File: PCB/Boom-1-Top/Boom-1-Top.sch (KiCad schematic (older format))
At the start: 983 parts, among them J1 DEBUG, J10 PIC_DEBUG, J11 PIC_DEBUG, J12 PIC_DEBUG, J13 PIC_DEBUG, J14 PIC_DEBUG, J15 USB_B_Micro, J16 SD_Card, J17 BT_DEBUG, J18 12V Supply, J19 3V3 Bypass, J2 MIDI IN, J20 5V Bypass, J21 Env +12V Supply, J22 Env -12V Supply, J23 OLEDConn, J3 MIDI OUT, J37 Osc1Conn, J38 Osc2Conn, J39 SubNoiseConn, J4 PIC_DEBUG, J40 FiltConn2, J41 EnvGenConn2, J42 EnvGenConn1, J43 FXConn1, J44 FiltConn1, J45 FXConn2, J46 EnvGenConn3, J5 PIC_DEBUG, J6 PIC_DEBUG, J7 PIC_DEBUG, J8 PIC_DEBUG, J9 PIC_DEBUG, Q1 AO3401A, Q2 AO3401A, SW1 Osc1SawEncoder, SW10 SubToOsc2FiltEncoder, SW11 Osc1ToOsc2FiltEncoder, SW12 Osc1FiltFreqEncoder, SW13 Osc2FiltFreqEncoder, SW14 SubFiltFreqEncoder, SW15 OscFiltEnvAttackEncoder, SW16 SubFiltEnvAttackEncoder, SW17 Osc1FiltResEncoder, SW18 Osc2FiltResEncoder, SW19 SubFiltResEncoder, SW2 Osc1SqrEncoder, SW20 OscFiltEnvDecayEncoder, SW21 SubFiltEnvDecayEncoder, SW22 OscFiltEnvSustainEncoder, SW23 SubFiltEnvSustainEncoder, SW24 Osc1DriveEncoder, SW25 Osc2DistortionEncoder, SW26 OscFiltEnvReleaseEncoder, SW27 SubFiltEnvReleaseEncoder, SW28 FXWetDryEncoder, SW29 SubAmpEnvAttackEncoder, SW3 Rotary_Encoder, SW30 OscAmpEnvAttackEncoder, SW31 FXControl1Encoder, SW32 SubAmpEnvDecayEncoder, SW33 OscAmpEnvDecayEncoder, SW34 FXControl2Encoder, SW35 SubAmpEnvSustainEncoder, SW36 OscAmpEnvSustainEncoder, SW37 FXControl3Encoder, SW38 FXFeedbackEncoder, SW39 SubAmpEnvReleaseEncoder, SW4 Rotary_Encoder_Switch, SW40 OscAmpEnvReleaseEncoder, SW41 Reset, SW42 SW_Push, SW43 Reset, SW44 SW_Push, SW45 SW_Push, SW46 SW_Push, SW47 SW_Push, SW48 SW_Push, SW49 SW_Push, SW5 Rotary_Encoder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

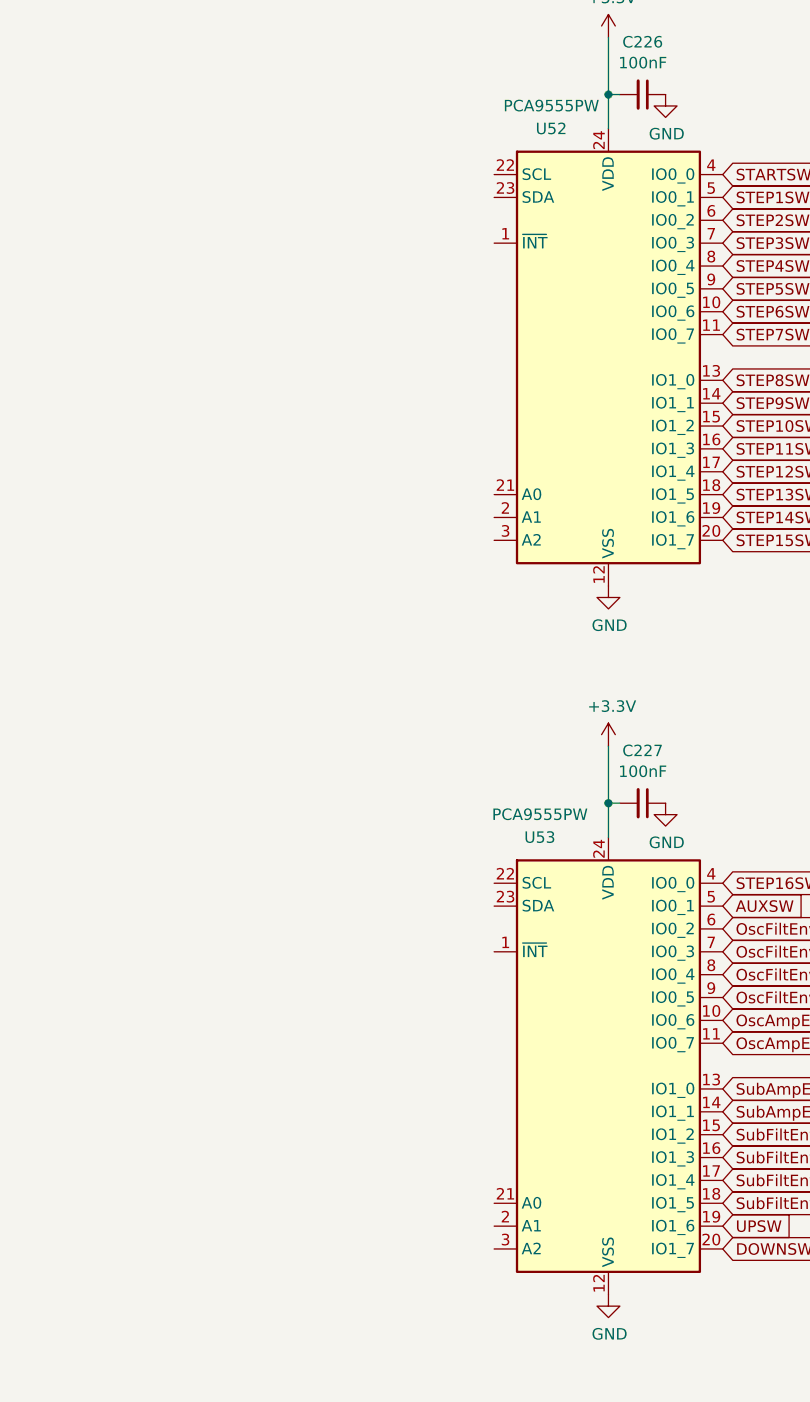
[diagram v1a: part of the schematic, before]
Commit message: - i2c lines for GPIO expanders - Tidied up 5v supply copper connection
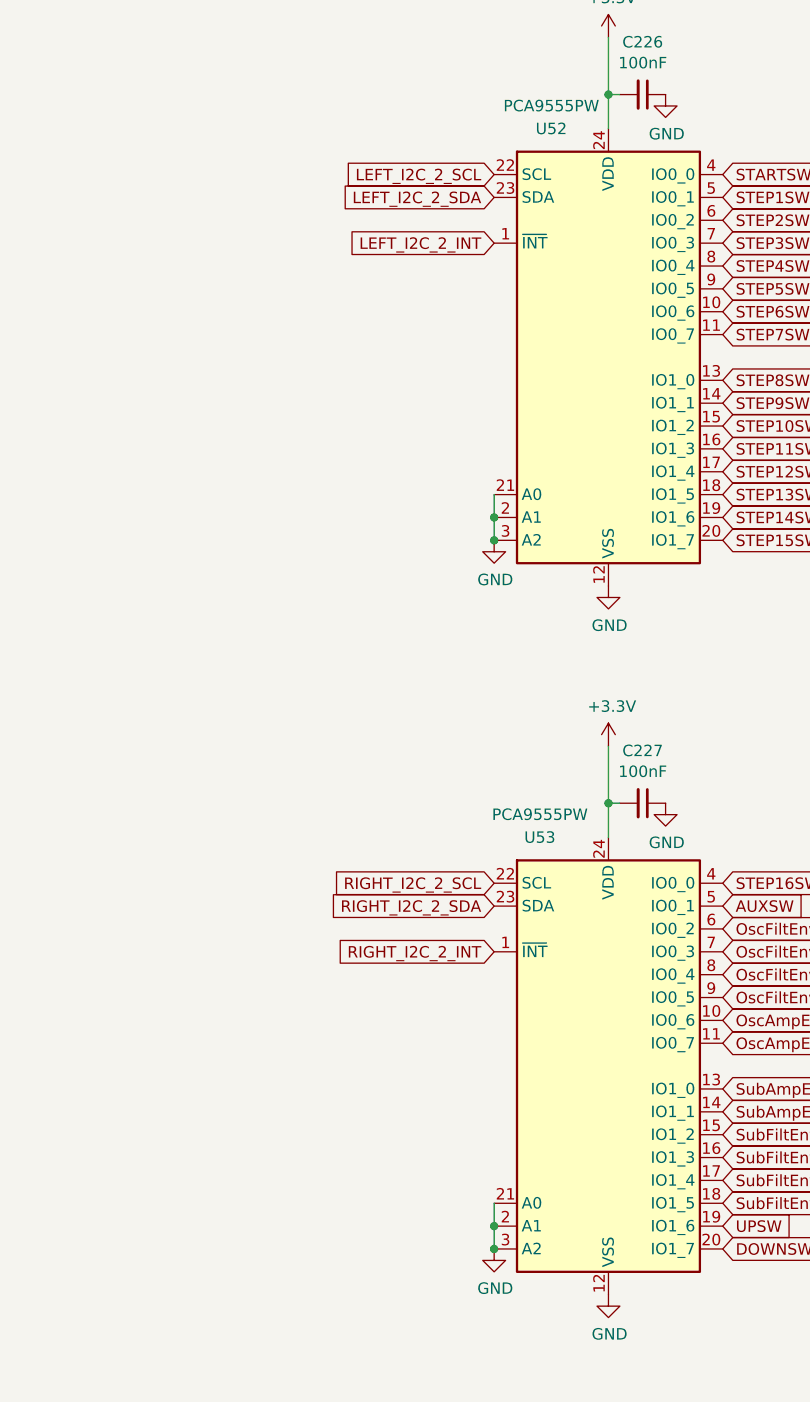
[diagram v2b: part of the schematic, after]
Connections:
- net GND: now also U52.2 (A1), U52.21 (A0), U52.3 (A2), U53.2 (A1), U53.21 (A0), U53.3 (A2)
- net LEFT_I2C_2_INT: now also U52.1 (~INT)
- net LEFT_I2C_2_SCL: now also U52.22 (SCL)
- net LEFT_I2C_2_SDA: now also U52.23 (SDA)
- net RIGHT_I2C_2_INT: now also U53.1 (~INT)
- net RIGHT_I2C_2_SCL: now also U53.22 (SCL)
- net RIGHT_I2C_2_SDA: now also U53.23 (SDA)
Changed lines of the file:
@@
 Wire Wire Line
 	5300 8800 5500 8800
+Text GLabel 21700 40750 0    50   Input ~ 0
+LEFT_I2C_2_SCL
+Text GLabel 21700 40850 0    50   Input ~ 0
+LEFT_I2C_2_SDA
+Text GLabel 21700 41050 0    50   Input ~ 0
+LEFT_I2C_2_INT
+Text GLabel 21700 43850 0    50   Input ~ 0
+RIGHT_I2C_2_SCL
+Text GLabel 21700 43950 0    50   Input ~ 0
+RIGHT_I2C_2_SDA
+Text GLabel 21700 44150 0    50   Input ~ 0
+RIGHT_I2C_2_INT
+$Comp
+L power:GND #PWR?
+U 1 1 6122B540
+P 21700 45450
+F 0 "#PWR?" H 21700 45200 50  0001 C CNN
+F 1 "GND" H 21705 45277 50  0000 C CNN
+F 2 "" H 21700 45450 50  0001 C CNN
+F 3 "" H 21700 45450 50  0001 C CNN
+	1    21700 45450
+	1    0    0    -1
+$EndComp
+Wire Wire Line
+	21700 45250 21700 45350
+Connection ~ 21700 45450
+Connection ~ 21700 45350
+Wire Wire Line
+	21700 45350 21700 45450
+$Comp
+L power:GND #PWR?
+U 1 1 617418BC
+P 21700 42350
+F 0 "#PWR?" H 21700 42100 50  0001 C CNN
+F 1 "GND" H 21705 42177 50  0000 C CNN
+F 2 "" H 21700 42350 50  0001 C CNN
+F 3 "" H 21700 42350 50  0001 C CNN
+	1    21700 42350
+	1    0    0    -1
+$EndComp
+Wire Wire Line
+	21700 42150 21700 42250
+Connection ~ 21700 42350
+Connection ~ 21700 42250
+Wire Wire Line
+	21700 42250 21700 42350
 $EndSCHEMATC

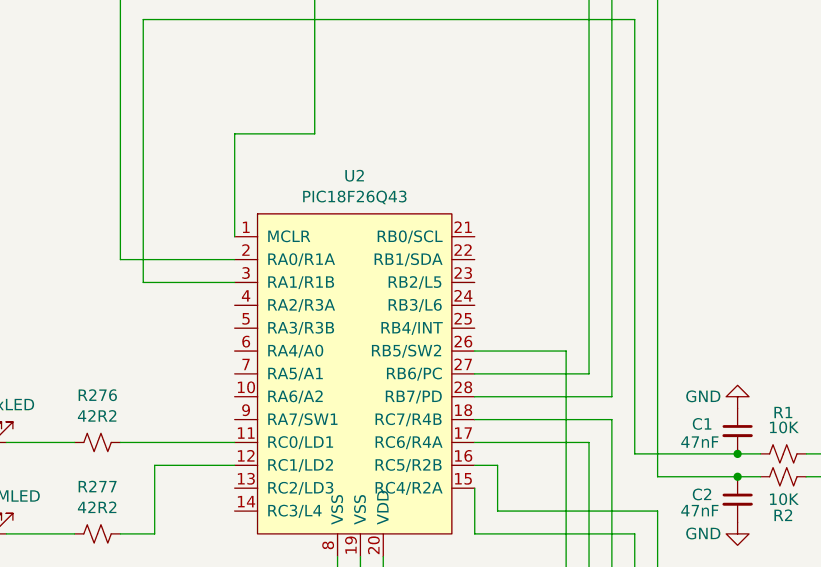
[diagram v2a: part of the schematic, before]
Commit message: First i2c line for PIC
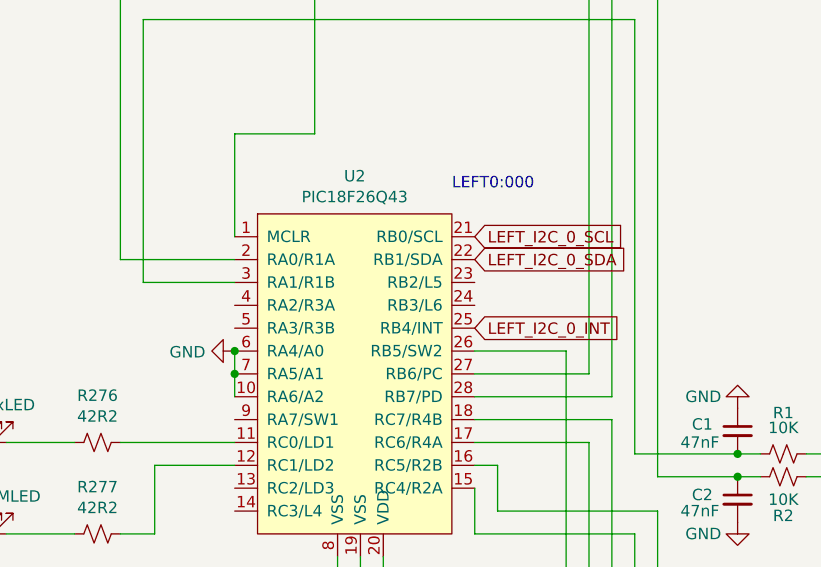
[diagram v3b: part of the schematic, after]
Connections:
- net GND: now also U2.10 (RA6/A2), U2.6 (RA4/A0), U2.7 (RA5/A1)
- net LEFT_I2C_0_INT: now also U2.25 (RB4/INT)
- net LEFT_I2C_0_SCL: now also U2.21 (RB0/SCL)
- net LEFT_I2C_0_SDA: now also U2.22 (RB1/SDA)
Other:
- note added: "LEFT0:000"
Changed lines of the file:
@@
 RIGHT_I2C_2_INT
 $Comp
-L power:GND #PWR?
+L power:GND #PWR0901
 U 1 1 6122B540
 P 21700 45450
-F 0 "#PWR?" H 21700 45200 50  0001 C CNN
+F 0 "#PWR0901" H 21700 45200 50  0001 C CNN
 F 1 "GND" H 21705 45277 50  0000 C CNN
 F 2 "" H 21700 45450 50  0001 C CNN
@@
 	21700 45350 21700 45450
 $Comp
-L power:GND #PWR?
+L power:GND #PWR0902
 U 1 1 617418BC
 P 21700 42350
-F 0 "#PWR?" H 21700 42100 50  0001 C CNN
+F 0 "#PWR0902" H 21700 42100 50  0001 C CNN
 F 1 "GND" H 21705 42177 50  0000 C CNN
 F 2 "" H 21700 42350 50  0001 C CNN
@@
 Wire Wire Line
 	21700 42250 21700 42350
+Text GLabel 27300 4400 2    50   Input ~ 0
+LEFT_I2C_0_SCL
+Text GLabel 27300 4500 2    50   Input ~ 0
+LEFT_I2C_0_SDA
+Text GLabel 27300 4800 2    50   Input ~ 0
+LEFT_I2C_0_INT
+Text Notes 27200 4200 0    50   ~ 0
+LEFT0:000
+$Comp
+L power:GND #PWR?
+U 1 1 637C74D9
+P 26250 4900
+F 0 "#PWR?" H 26250 4650 50  0001 C CNN
+F 1 "GND" V 26255 4772 50  0000 R CNN
+F 2 "" H 26250 4900 50  0001 C CNN
+F 3 "" H 26250 4900 50  0001 C CNN
+	1    26250 4900
+	0    1    1    0
+$EndComp
+Wire Wire Line
+	26250 4900 26250 5000
+Connection ~ 26250 4900
+Connection ~ 26250 5000
+Wire Wire Line
+	26250 5000 26250 5100
 $EndSCHEMATC

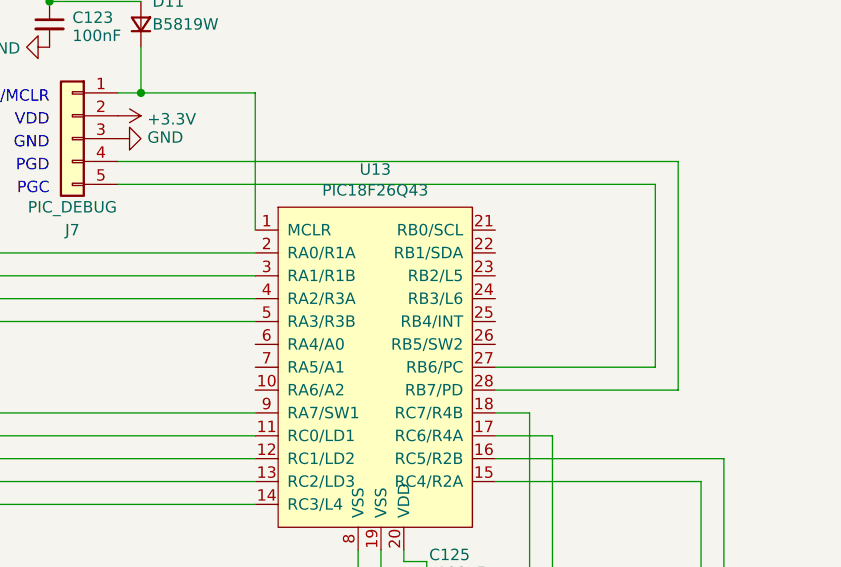
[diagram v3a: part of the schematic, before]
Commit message: i2c for PIC U13
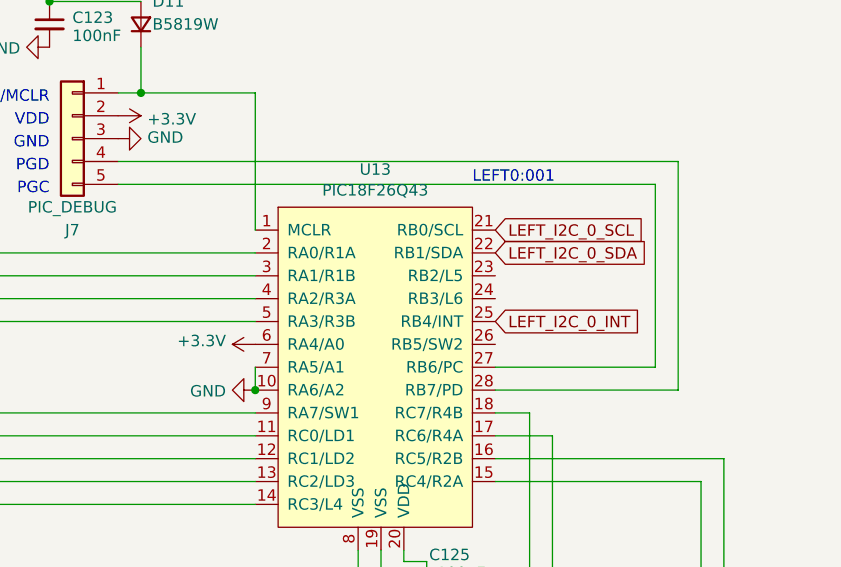
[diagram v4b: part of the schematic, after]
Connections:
- net +3V3: now also U13.6 (RA4/A0)
- net GND: now also U13.10 (RA6/A2), U13.7 (RA5/A1)
- net LEFT_I2C_0_INT: now also U13.25 (RB4/INT)
- net LEFT_I2C_0_SCL: now also U13.21 (RB0/SCL)
- net LEFT_I2C_0_SDA: now also U13.22 (RB1/SDA)
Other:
- note added: "LEFT0:001"
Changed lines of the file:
@@
 Wire Wire Line
 	21700 42250 21700 42350
-Text GLabel 27300 4400 2    50   Input ~ 0
-LEFT_I2C_0_SCL
-Text GLabel 27300 4500 2    50   Input ~ 0
-LEFT_I2C_0_SDA
-Text GLabel 27300 4800 2    50   Input ~ 0
-LEFT_I2C_0_INT
 Text Notes 27200 4200 0    50   ~ 0
 LEFT0:000
 $Comp
-L power:GND #PWR?
+L power:GND #PWR0903
 U 1 1 637C74D9
 P 26250 4900
-F 0 "#PWR?" H 26250 4650 50  0001 C CNN
+F 0 "#PWR0903" H 26250 4650 50  0001 C CNN
 F 1 "GND" V 26255 4772 50  0000 R CNN
 F 2 "" H 26250 4900 50  0001 C CNN
@@
 Wire Wire Line
 	26250 5000 26250 5100
+Text GLabel 27300 4800 2    50   Input ~ 0
+LEFT_I2C_0_INT
+Text GLabel 27300 4500 2    50   Input ~ 0
+LEFT_I2C_0_SDA
+Text GLabel 27300 4400 2    50   Input ~ 0
+LEFT_I2C_0_SCL
+Text Notes 35800 2200 0    50   ~ 0
+LEFT0:001
+Text GLabel 35900 2800 2    50   Input ~ 0
+LEFT_I2C_0_INT
+Text GLabel 35900 2500 2    50   Input ~ 0
+LEFT_I2C_0_SDA
+Text GLabel 35900 2400 2    50   Input ~ 0
+LEFT_I2C_0_SCL
+$Comp
+L power:+3.3V #PWR?
+U 1 1 60D460BD
+P 34850 2900
+F 0 "#PWR?" H 34850 2750 50  0001 C CNN
+F 1 "+3.3V" V 34865 3028 50  0000 L CNN
+F 2 "" H 34850 2900 50  0001 C CNN
+F 3 "" H 34850 2900 50  0001 C CNN
+	1    34850 2900
+	0    -1   -1   0
+$EndComp
+$Comp
+L power:GND #PWR?
+U 1 1 60D5214D
+P 34850 3100
+F 0 "#PWR?" H 34850 2850 50  0001 C CNN
+F 1 "GND" V 34855 2972 50  0000 R CNN
+F 2 "" H 34850 3100 50  0001 C CNN
+F 3 "" H 34850 3100 50  0001 C CNN
+	1    34850 3100
+	0    1    1    0
+$EndComp
+Wire Wire Line
+	34850 3100 34850 3000
+Connection ~ 34850 3100
 $EndSCHEMATC

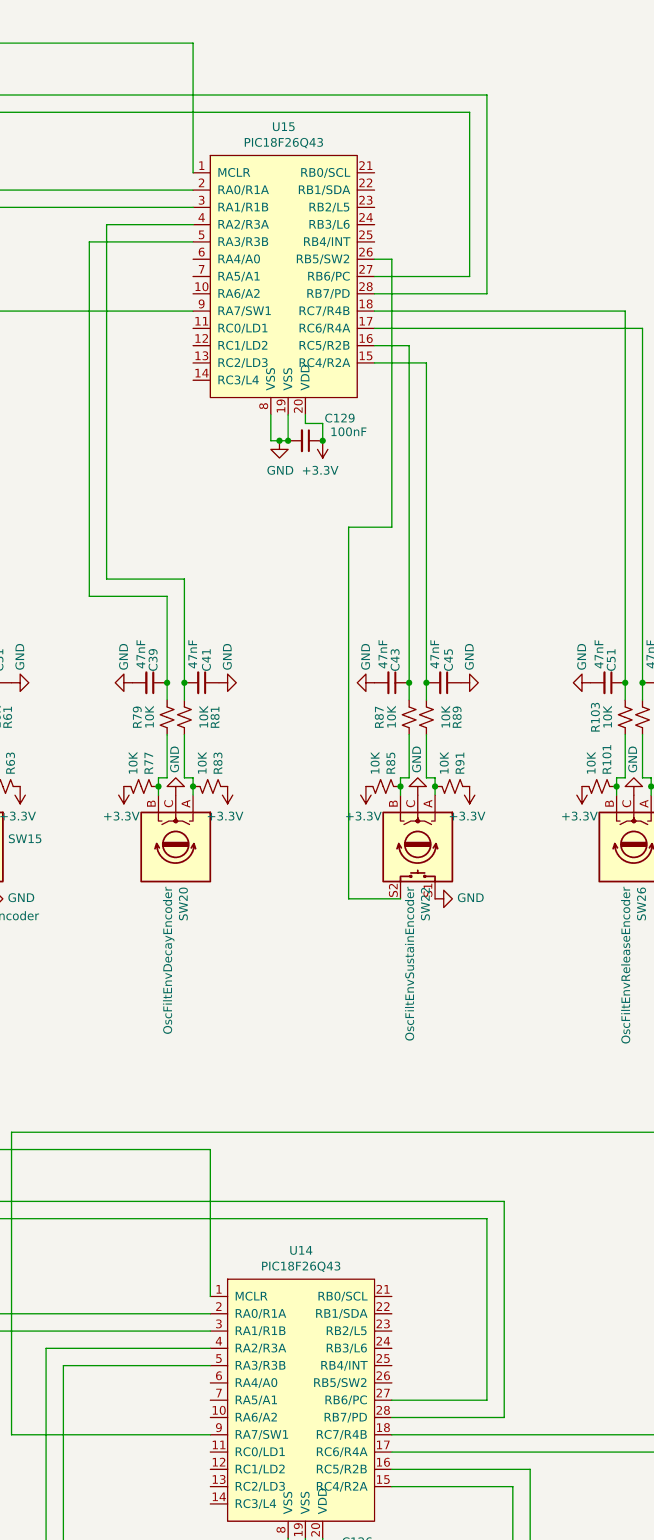
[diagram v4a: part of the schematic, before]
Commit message: i2c for PIC U14
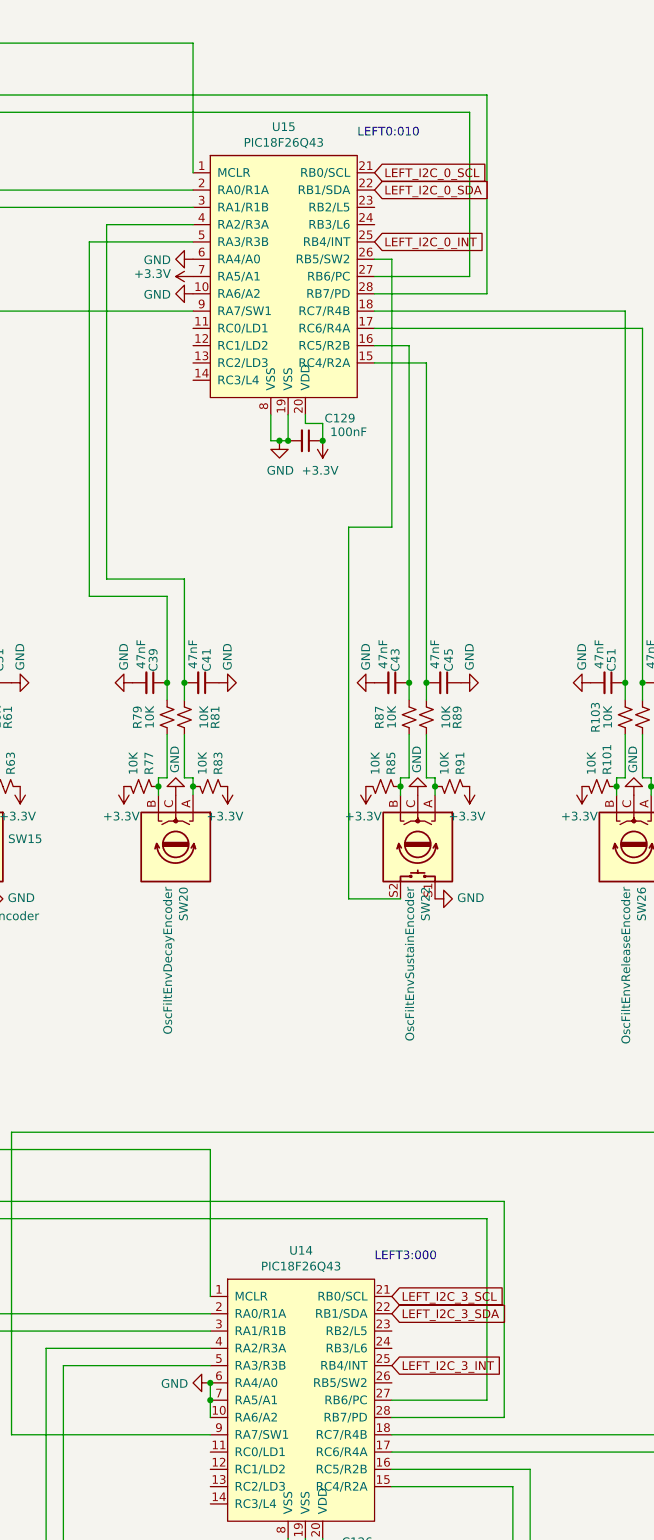
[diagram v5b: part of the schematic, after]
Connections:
- net +3V3: now also U15.7 (RA5/A1)
- net GND: now also U14.10 (RA6/A2), U14.6 (RA4/A0), U14.7 (RA5/A1), U15.10 (RA6/A2), U15.6 (RA4/A0)
- net LEFT_I2C_0_INT: now also U15.25 (RB4/INT)
- net LEFT_I2C_0_SCL: now also U15.21 (RB0/SCL)
- net LEFT_I2C_0_SDA: now also U15.22 (RB1/SDA)
- net LEFT_I2C_3_INT: now also U14.25 (RB4/INT)
- net LEFT_I2C_3_SCL: now also U14.21 (RB0/SCL)
- net LEFT_I2C_3_SDA: now also U14.22 (RB1/SDA)
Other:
- note added: "LEFT0:010"
- note added: "LEFT3:000"
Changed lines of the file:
@@
 LEFT_I2C_0_SCL
 $Comp
-L power:+3.3V #PWR?
+L power:+3.3V #PWR0904
 U 1 1 60D460BD
 P 34850 2900
-F 0 "#PWR?" H 34850 2750 50  0001 C CNN
+F 0 "#PWR0904" H 34850 2750 50  0001 C CNN
 F 1 "+3.3V" V 34865 3028 50  0000 L CNN
 F 2 "" H 34850 2900 50  0001 C CNN
@@
 $EndComp
 $Comp
-L power:GND #PWR?
+L power:GND #PWR0905
 U 1 1 60D5214D
 P 34850 3100
-F 0 "#PWR?" H 34850 2850 50  0001 C CNN
+F 0 "#PWR0905" H 34850 2850 50  0001 C CNN
 F 1 "GND" V 34855 2972 50  0000 R CNN
 F 2 "" H 34850 3100 50  0001 C CNN
@@
 	34850 3100 34850 3000
 Connection ~ 34850 3100
+Text Notes 38500 7450 0    50   ~ 0
+LEFT0:010
+Text GLabel 38600 8050 2    50   Input ~ 0
+LEFT_I2C_0_INT
+Text GLabel 38600 7750 2    50   Input ~ 0
+LEFT_I2C_0_SDA
+Text GLabel 38600 7650 2    50   Input ~ 0
+LEFT_I2C_0_SCL
+$Comp
+L power:GND #PWR0906
+U 1 1 6194E624
+P 37550 8150
+F 0 "#PWR0906" H 37550 7900 50  0001 C CNN
+F 1 "GND" V 37555 8022 50  0000 R CNN
+F 2 "" H 37550 8150 50  0001 C CNN
+F 3 "" H 37550 8150 50  0001 C CNN
+	1    37550 8150
+	0    1    1    0
+$EndComp
+$Comp
+L power:+3.3V #PWR0907
+U 1 1 6195A0B4
+P 37550 8250
+F 0 "#PWR0907" H 37550 8100 50  0001 C CNN
+F 1 "+3.3V" V 37565 8378 50  0000 L CNN
+F 2 "" H 37550 8250 50  0001 C CNN
+F 3 "" H 37550 8250 50  0001 C CNN
+	1    37550 8250
+	0    -1   -1   0
+$EndComp
+$Comp
+L power:GND #PWR0908
+U 1 1 61965D63
+P 37550 8350
+F 0 "#PWR0908" H 37550 8100 50  0001 C CNN
+F 1 "GND" V 37555 8222 50  0000 R CNN
+F 2 "" H 37550 8350 50  0001 C CNN
+F 3 "" H 37550 8350 50  0001 C CNN
+	1    37550 8350
+	0    1    1    0
+$EndComp
+Text Notes 38600 13950 0    50   ~ 0
+LEFT3:000
+Text GLabel 38700 14550 2    50   Input ~ 0
+LEFT_I2C_3_INT
+Text GLabel 38700 14250 2    50   Input ~ 0
+LEFT_I2C_3_SDA
+Text GLabel 38700 14150 2    50   Input ~ 0
+LEFT_I2C_3_SCL
+$Comp
+L power:GND #PWR?
+U 1 1 62205F51
+P 37650 14650
+F 0 "#PWR?" H 37650 14400 50  0001 C CNN
+F 1 "GND" V 37655 14522 50  0000 R CNN
+F 2 "" H 37650 14650 50  0001 C CNN
+F 3 "" H 37650 14650 50  0001 C CNN
+	1    37650 14650
+	0    1    1    0
+$EndComp
+Wire Wire Line
+	37650 14650 37650 14750
+Connection ~ 37650 14650
+Connection ~ 37650 14750
+Wire Wire Line
+	37650 14750 37650 14850
 $EndSCHEMATC

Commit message: U19 PIC i2c
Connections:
- net GND: now also U19.10 (RA6/A2), U19.6 (RA4/A0), U19.7 (RA5/A1)
- net RIGHT_I2C_0_INT: now also U19.25 (RB4/INT)
- net RIGHT_I2C_0_SCL: now also U19.21 (RB0/SCL)
- net RIGHT_I2C_0_SDA: now also U19.22 (RB1/SDA)
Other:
- note added: "RIGHT0:000"
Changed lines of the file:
@@
 Wire Wire Line
 	37650 14750 37650 14850
+Text GLabel 45300 2650 2    50   Input ~ 0
+RIGHT_I2C_0_SDA
+Text GLabel 45300 2550 2    50   Input ~ 0
+RIGHT_I2C_0_SCL
+Text GLabel 45300 2950 2    50   Input ~ 0
+RIGHT_I2C_0_INT
+Text Notes 45350 2450 0    50   ~ 0
+RIGHT0:000
+$Comp
+L power:GND #PWR?
+U 1 1 60DF9D17
+P 44250 3050
+F 0 "#PWR?" H 44250 2800 50  0001 C CNN
+F 1 "GND" V 44255 2922 50  0000 R CNN
+F 2 "" H 44250 3050 50  0001 C CNN
+F 3 "" H 44250 3050 50  0001 C CNN
+	1    44250 3050
+	0    1    1    0
+$EndComp
+Wire Wire Line
+	44250 3050 44250 3150
+Connection ~ 44250 3050
+Connection ~ 44250 3150
+Wire Wire Line
+	44250 3150 44250 3250
 $EndSCHEMATC
